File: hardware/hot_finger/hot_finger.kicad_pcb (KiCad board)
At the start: 2 copper layers, 34 parts, among them J1 USB_C_Receptacle_USB2.0, Q1 2N7002, Q2 2N7002, Q3 2N7002, Q4 2N7002, Q5 2N7002, Q6 2N7002, Q7 2N7002, Q8 2N7002, U1 RP2040

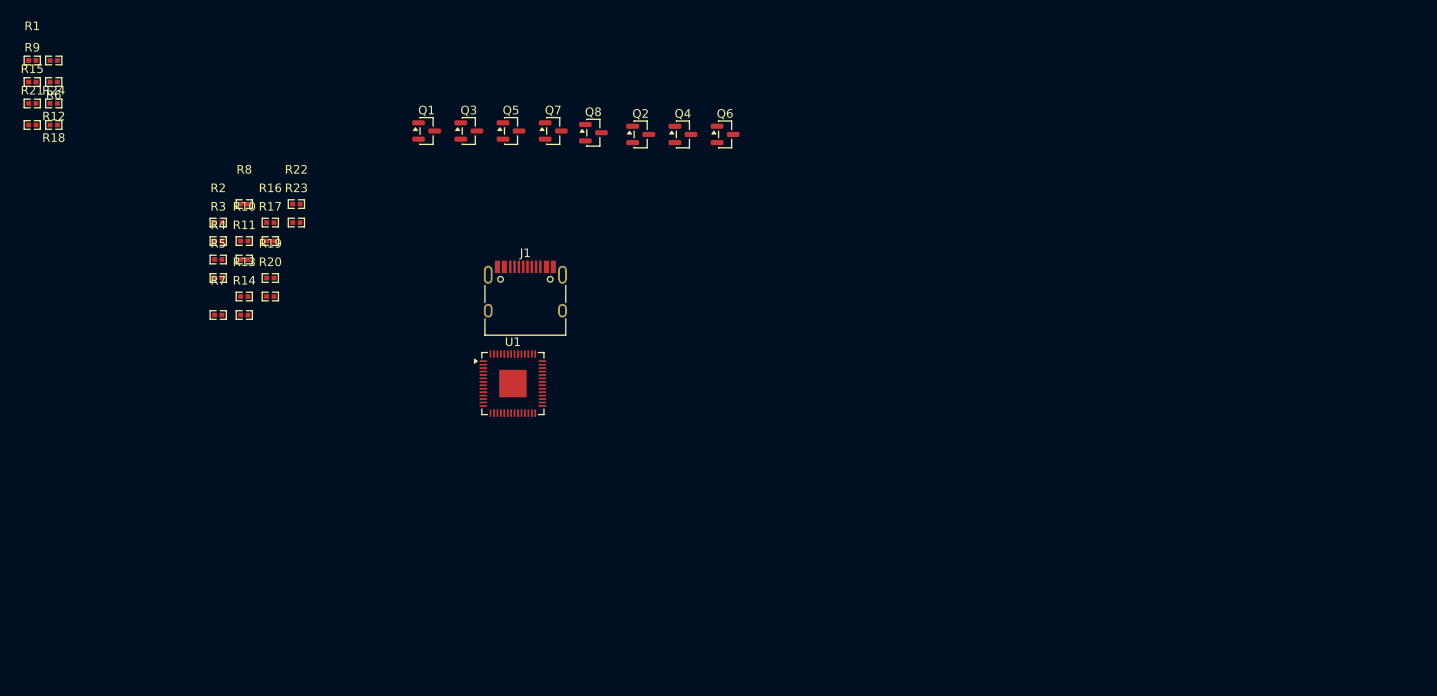
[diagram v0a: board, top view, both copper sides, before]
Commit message: feature: add photodiodes
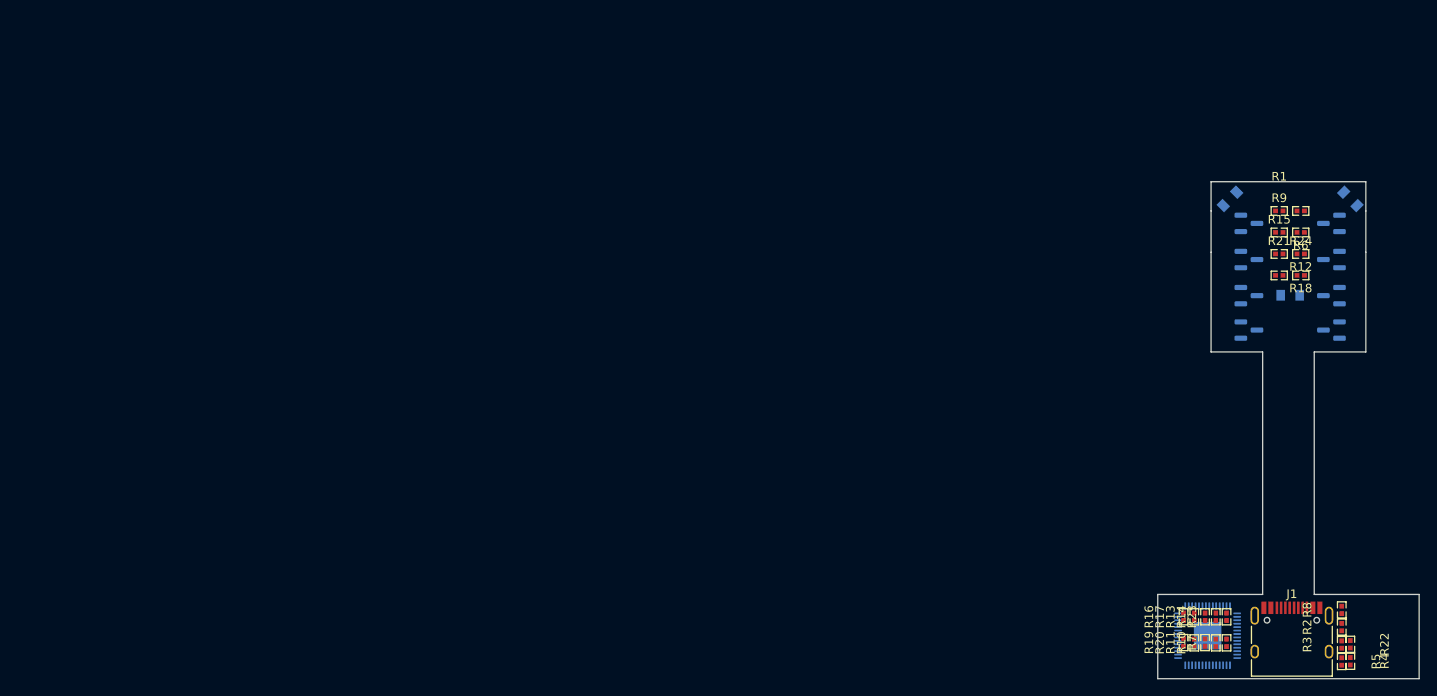
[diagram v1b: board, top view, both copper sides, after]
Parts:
- added U2: TEMD6200FX01, easyeda2kicad:OPTO-SMD_L2.0-W1.3-RD-1, B.Cu at (165.2, 36.6)
- added U3: TEMD6200FX01, easyeda2kicad:OPTO-SMD_L2.0-W1.3-RD-1, B.Cu at (179.2, 36.6)
- added U4: TEMD6200FX01, easyeda2kicad:OPTO-SMD_L2.0-W1.3-RD-1, B.Cu at (172.2, 47.8)
- Q1, Q2, Q3, Q4, Q5, Q6, Q7, Q8, U1: moved to B.Cu
- moved R1 146.1 mm to (170.9, 38.0)
- moved R12 146.1 mm to (173.4, 40.5)
- moved R15 146.1 mm to (170.9, 43.0)
- moved R18 146.1 mm to (173.4, 43.0)
- moved R21 146.1 mm to (170.9, 45.5)
- moved R24 146.1 mm to (173.4, 45.5)
- moved R6 146.1 mm to (173.4, 38.0)
- moved R9 146.1 mm to (170.9, 40.5)
- moved R4 139.7 mm to (179.2, 90.4), turned to -90 degrees
- moved R2 138.9 mm to (178.2, 86.4), turned to 90 degrees
- moved R3 138.8 mm to (178.2, 88.4), turned to 90 degrees
- moved R5 138.1 mm to (178.2, 90.4), turned to -90 degrees
- moved R8 136.1 mm to (178.2, 84.4), turned to 90 degrees
- moved R22 132.8 mm to (179.2, 88.4), turned to -90 degrees
- moved R7 123.3 mm to (164.8, 88.2), turned to 90 degrees
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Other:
- board outline added: 30.4 x 57.8 mm
